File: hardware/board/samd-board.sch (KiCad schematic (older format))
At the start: 26 parts, among them J1 USB_B_Mini, J2 Conn_ARM_JTAG_SWD_10, J3 Conn_01x16_Male, J4 Conn_01x16_Male, SW1 SW_Push, U1 AZ1117-3.3, U2 ATSAMD21E17D-A, Y1 8MHz

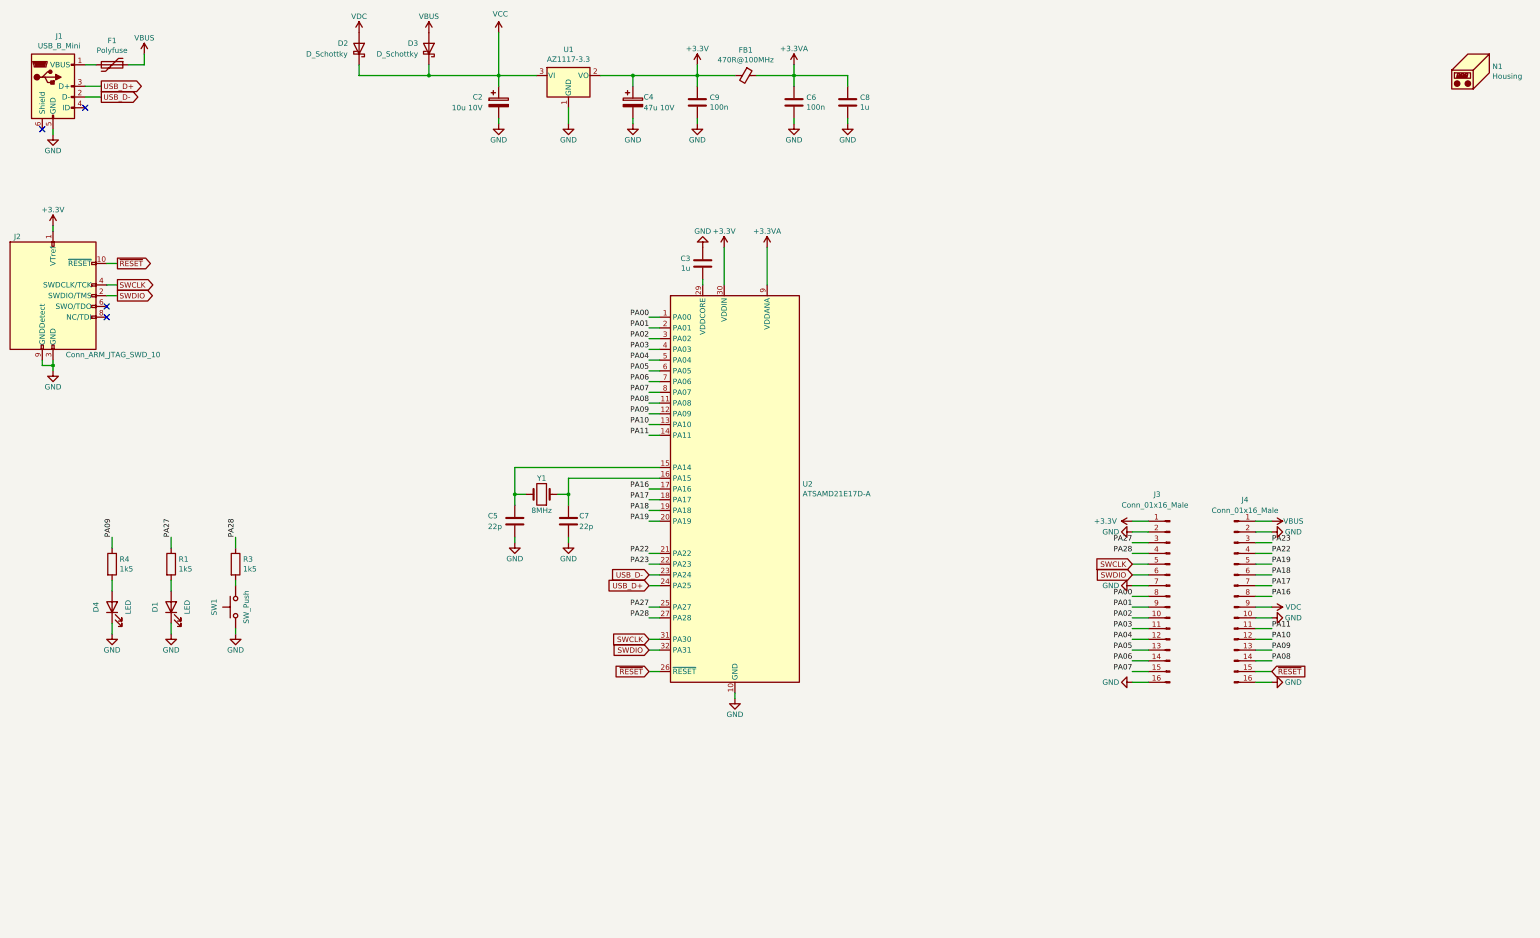
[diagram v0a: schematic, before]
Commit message: complete component silkscreen placement
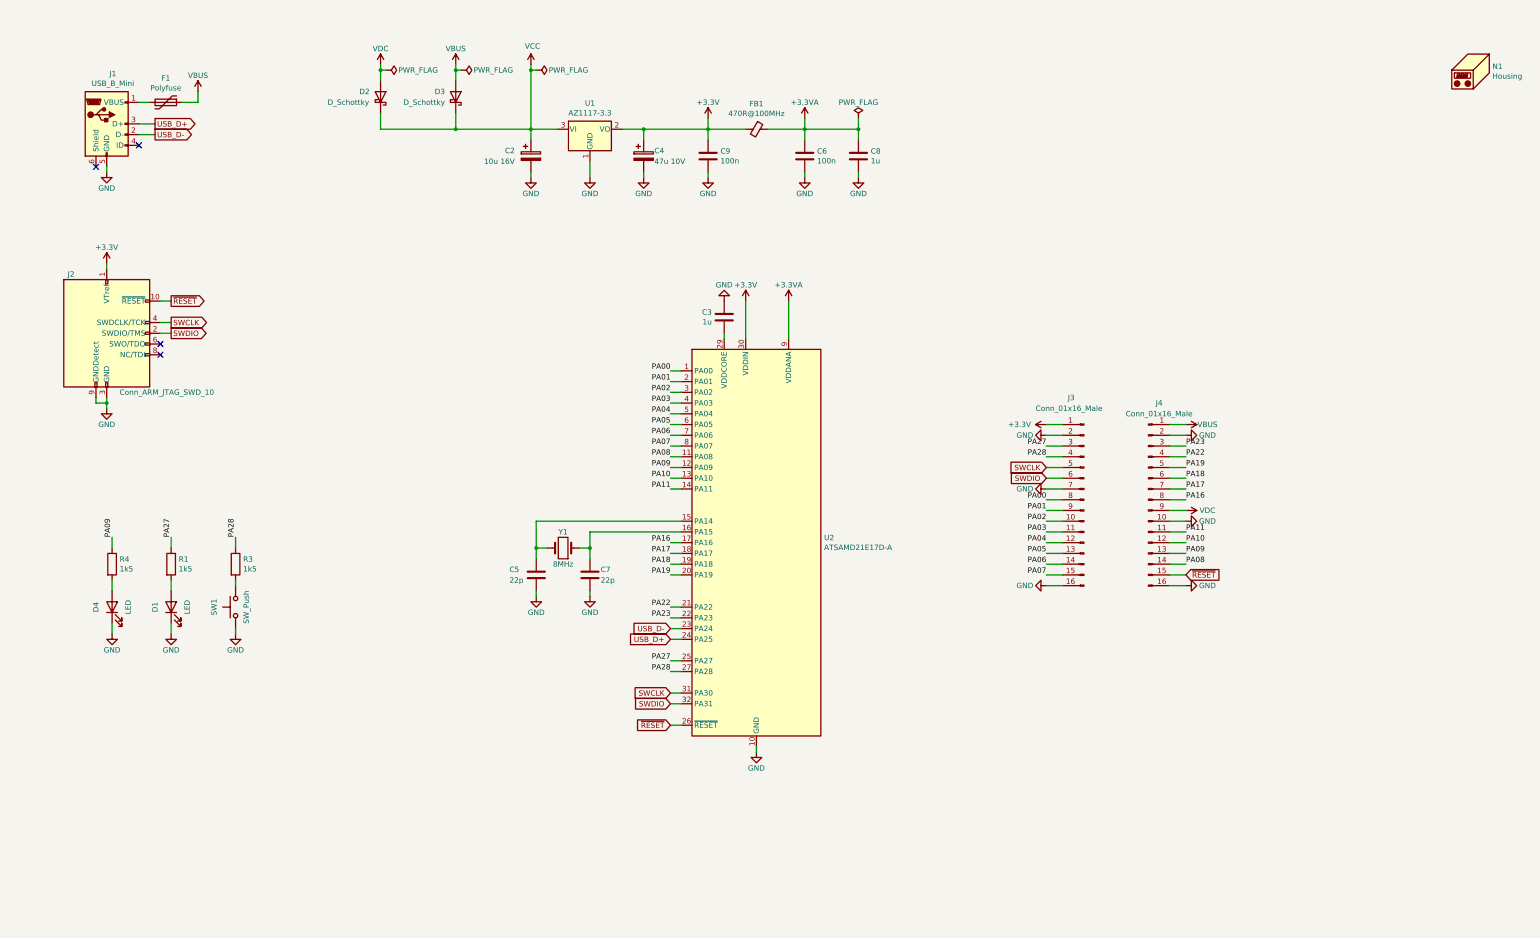
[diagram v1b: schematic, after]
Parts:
- C2: value 10u 10V -> 10u 16V
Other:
- moved on the sheet: C2, C3, C4, C5, C6, C7, C8, C9, D2, D3, F1, FB1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

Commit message: add power LED, pin silkscreen markers
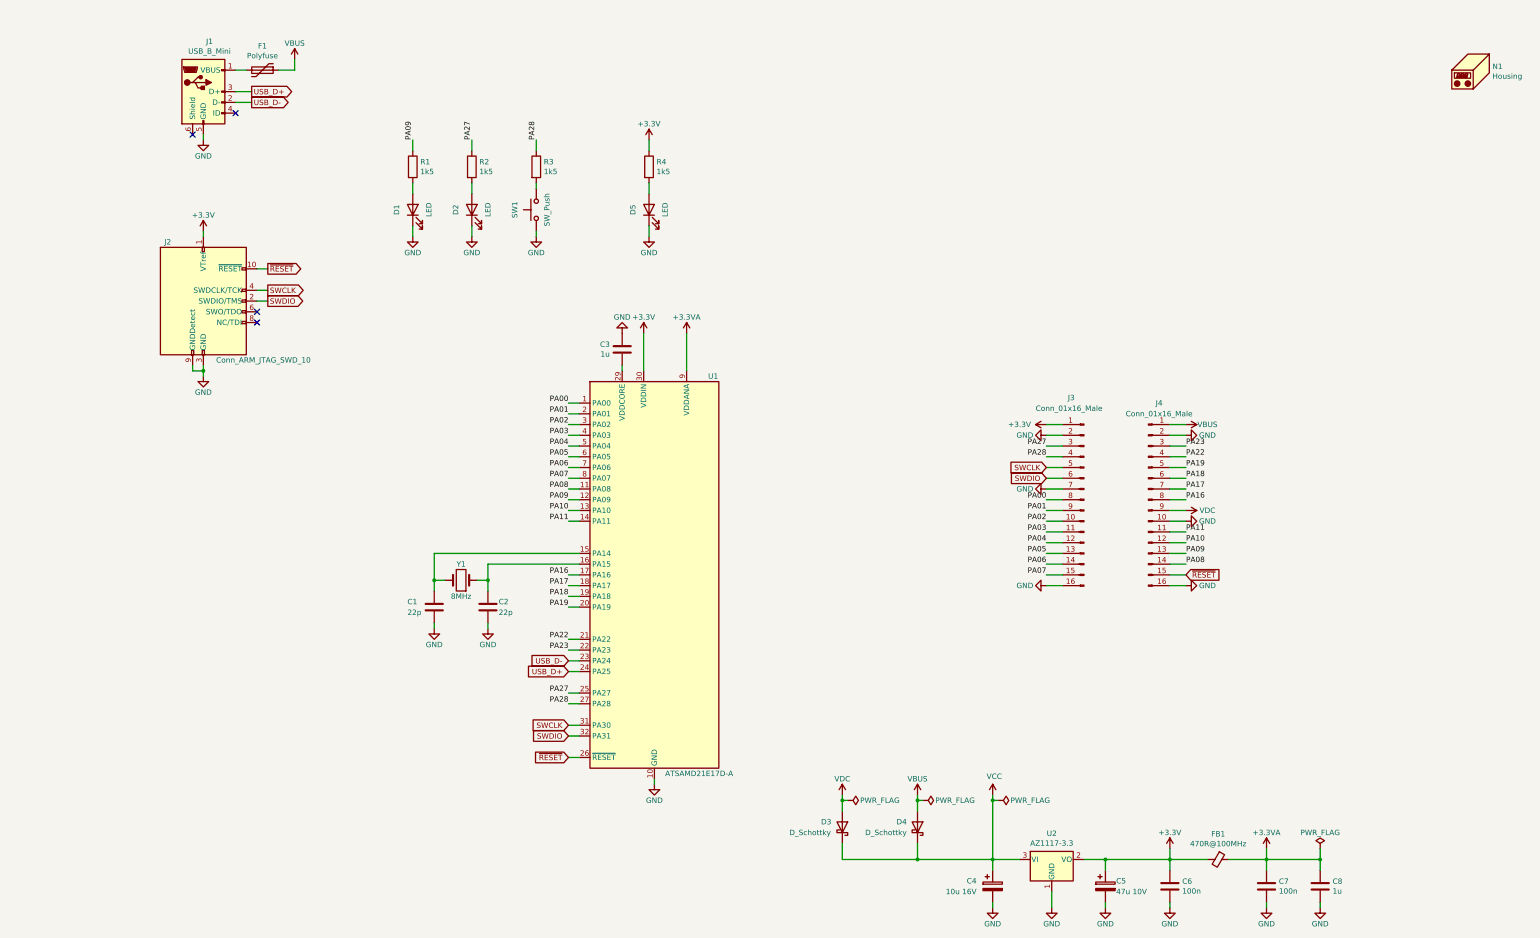
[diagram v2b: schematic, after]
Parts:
- added D5: LED, Assorted:LED_0603_1608Metric_Pad1.05x0.95mm_HandSolder, symbol Device:LED
- added R4: 1k5, Resistor_SMD:R_0603_1608Metric_Pad0.98x0.95mm_HandSolder, symbol Device:R
- D1: renamed from D4; footprint LED_SMD:LED_0603_1608Metric_Pad1.05x0.95mm_HandSolder -> Assorted:LED_0603_1608Metric_Pad1.05x0.95mm_HandSolder
- D2: renamed from D1; footprint LED_SMD:LED_0603_1608Metric_Pad1.05x0.95mm_HandSolder -> Assorted:LED_0603_1608Metric_Pad1.05x0.95mm_HandSolder
- renumbered C5 to C1, C7 to C2, C2 to C4, C4 to C5, C9 to C6, C6 to C7, D2 to D3, D3 to D4, R4 to R1, R1 to R2, U2 to U1, U1 to U2
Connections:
- net +3V3: now also R4.1
- net GND: now also D5.1 (K)
- new net: D5.2 (A), R4.2
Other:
- moved on the sheet: C1, C2, C3, C4, C5, C6, C7, C8, D1, D2, D3, D4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

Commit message: complete board
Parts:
- removed N1: Housing, Assorted:Template_Breadboard, symbol Mechanical:Housing
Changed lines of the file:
@@
 P 7150 6150
 F 0 "U1" H 7650 8000 50  0000 L CNN
-F 1 "ATSAMD21E17D-A" H 7250 4300 50  0000 L CNN
+F 1 "ATSAMD21E17D-A" H 7300 4300 50  0000 L CNN
 F 2 "Package_QFP:TQFP-32_7x7mm_P0.8mm" H 8050 4300 50  0001 C CNN
 F 3 "http://ww1.microchip.com/downloads/en/DeviceDoc/SAM_D21_DA1_Family_Data%20Sheet_DS40001882E.pdf" H 7150 6150 50  0001 C CNN
@@
 	-1   0    0    1
 $EndComp
-$Comp
-L Mechanical:Housing N1
-U 1 1 60E2C29B
-P 14800 1450
-F 0 "N1" H 14953 1484 50  0000 L CNN
-F 1 "Housing" H 14953 1393 50  0000 L CNN
-F 2 "Assorted:Template_Breadboard" H 14850 1500 50  0001 C CNN
-F 3 "~" H 14850 1500 50  0001 C CNN
-	1    14800 1450
-	1    0    0    -1
-$EndComp
 Wire Wire Line
